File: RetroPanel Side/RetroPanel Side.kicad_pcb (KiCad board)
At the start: 2 copper layers, 100 x 25 mm, 13 parts, among them M1 Mounting_Pin, M10 Mounting_Pad, M11 Mounting_Pad, M12 Mounting_Pad, M13 Mounting_Pad, M2 Mounting_Pin, M3 Mounting_Pin, M4 Mounting_Pad, M5 Mounting_Pad, M6 Mounting_Pad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

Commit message: Rough layout of module
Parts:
- moved M10 4.85 mm to (103.8, 98.5), turned to 270 degrees
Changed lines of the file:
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@@
   )
   (module RetroPanel:Pad_pin (layer F.Cu)
-    (at 103.0916 93.6898 180)
+    (at 103.8155 98.4904 270)
     (descr "module 1 pin (ou trou mecanique de percage)")
     (tags DEV)
-    (fp_text reference M10 (at 0 -4.445) (layer F.Fab) hide
+    (fp_text reference M10 (at 0 -4.445 90) (layer F.Fab) hide
       (effects (font (size 1 1) (thickness 0.15)))
     )
-    (fp_text value Mounting_Pad (at 0 -3.175) (layer F.Fab) hide
+    (fp_text value Mounting_Pad (at 0 -3.175 90) (layer F.Fab) hide
       (effects (font (size 1 1) (thickness 0.15)))
     )
-    (pad 1 smd rect (at 0 0 180) (size 3 4.4) (layers B.Cu B.Paste B.Mask)
+    (pad 1 smd rect (at 0 0 270) (size 3 4.4) (layers B.Cu B.Paste B.Mask)
       (net 1 GND))
-    (pad 1 smd rect (at 0 0 180) (size 3 4.4) (layers F.Cu F.Paste F.Mask)
+    (pad 1 smd rect (at 0 0 270) (size 3 4.4) (layers F.Cu F.Paste F.Mask)
       (net 1 GND))
   )
@@
       (effects (font (size 1 1) (thickness 0.15)))
     )
+    (fp_circle (center 0 0) (end 2.6 0) (layer F.CrtYd) (width 0.05))
     (fp_circle (center 0 0) (end 2 0.8) (layer F.Fab) (width 0.1))
-    (fp_circle (center 0 0) (end 2.6 0) (layer F.CrtYd) (width 0.05))
     (pad 1 thru_hole circle (at 0 0) (size 3.5 3.5) (drill 3.048) (layers *.Cu *.Mask)
       (net 1 GND) (solder_mask_margin 0.8))
@@
       (effects (font (size 1 1) (thickness 0.15)))
     )
+    (fp_circle (center 0 0) (end 2 0.8) (layer F.Fab) (width 0.1))
     (fp_circle (center 0 0) (end 2.6 0) (layer F.CrtYd) (width 0.05))
-    (fp_circle (center 0 0) (end 2 0.8) (layer F.Fab) (width 0.1))
     (pad 1 thru_hole circle (at 0 0) (size 3.5 3.5) (drill 3.048) (layers *.Cu *.Mask)
       (net 1 GND) (solder_mask_margin 0.8))
@@
       (effects (font (size 1 1) (thickness 0.15)))
     )
+    (fp_circle (center 0 0) (end 2 0.8) (layer F.Fab) (width 0.1))
     (fp_circle (center 0 0) (end 2.6 0) (layer F.CrtYd) (width 0.05))
-    (fp_circle (center 0 0) (end 2 0.8) (layer F.Fab) (width 0.1))
     (pad 1 thru_hole circle (at 0 0) (size 3.5 3.5) (drill 3.048) (layers *.Cu *.Mask)
       (net 1 GND) (solder_mask_margin 0.8))

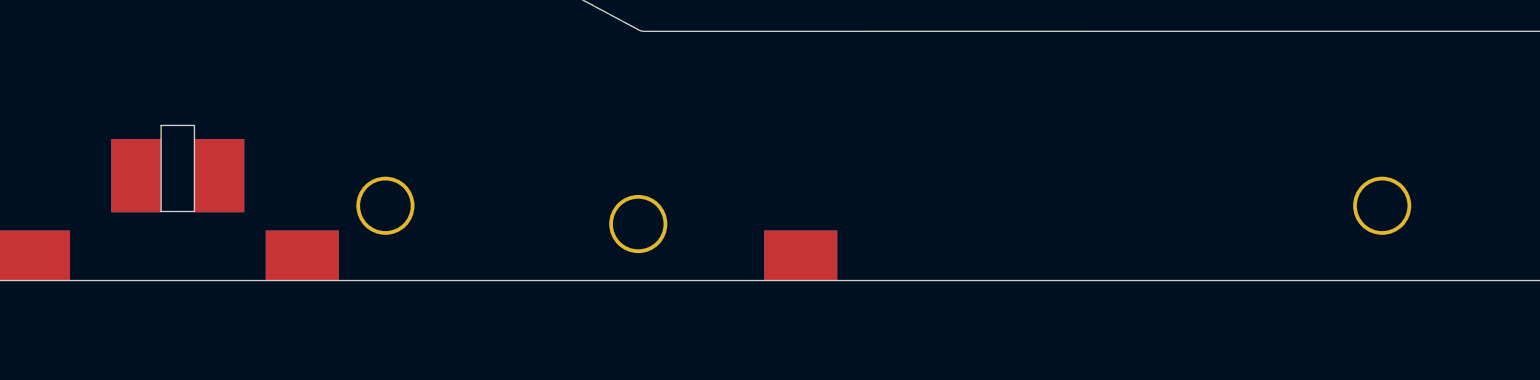
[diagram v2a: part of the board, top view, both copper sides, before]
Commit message: Adjustable mounting with huge pads
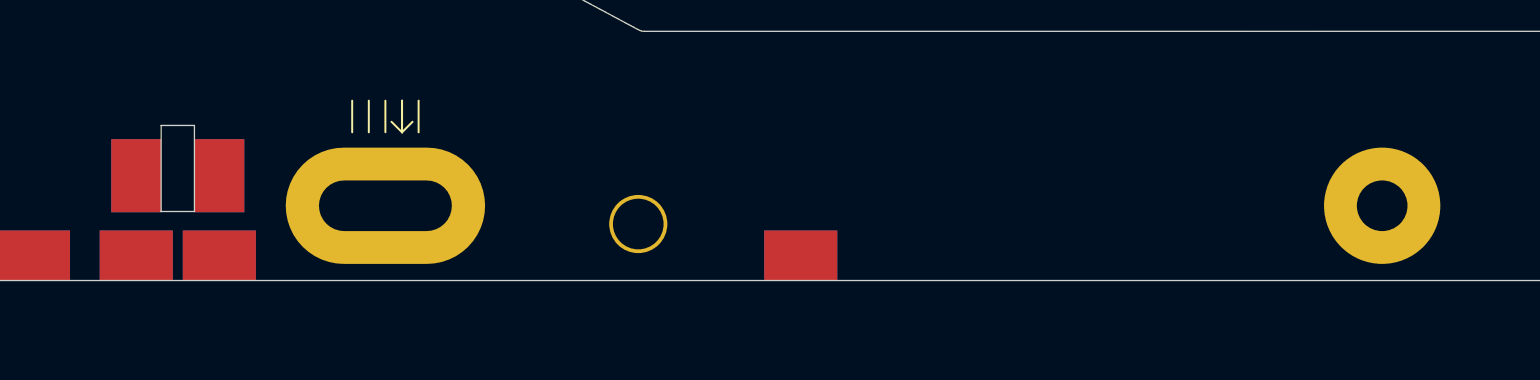
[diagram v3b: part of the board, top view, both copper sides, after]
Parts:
- added M14: Mounting_Pad, RetroPanel:Pad_pin, F.Cu at (110.0, 98.5)
- M1: footprint mounting:M3_pin -> mounting:M3_adjustable
- M2: footprint mounting:M3_pin -> mounting:M3_big
- moved M6 5.00 mm to (115.0, 98.5)
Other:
- board text added: "RetroPanel Side (rev. B) github.com/tebl"
- board text removed: "RetroPanel Side (rev. A) github.com/tebl"

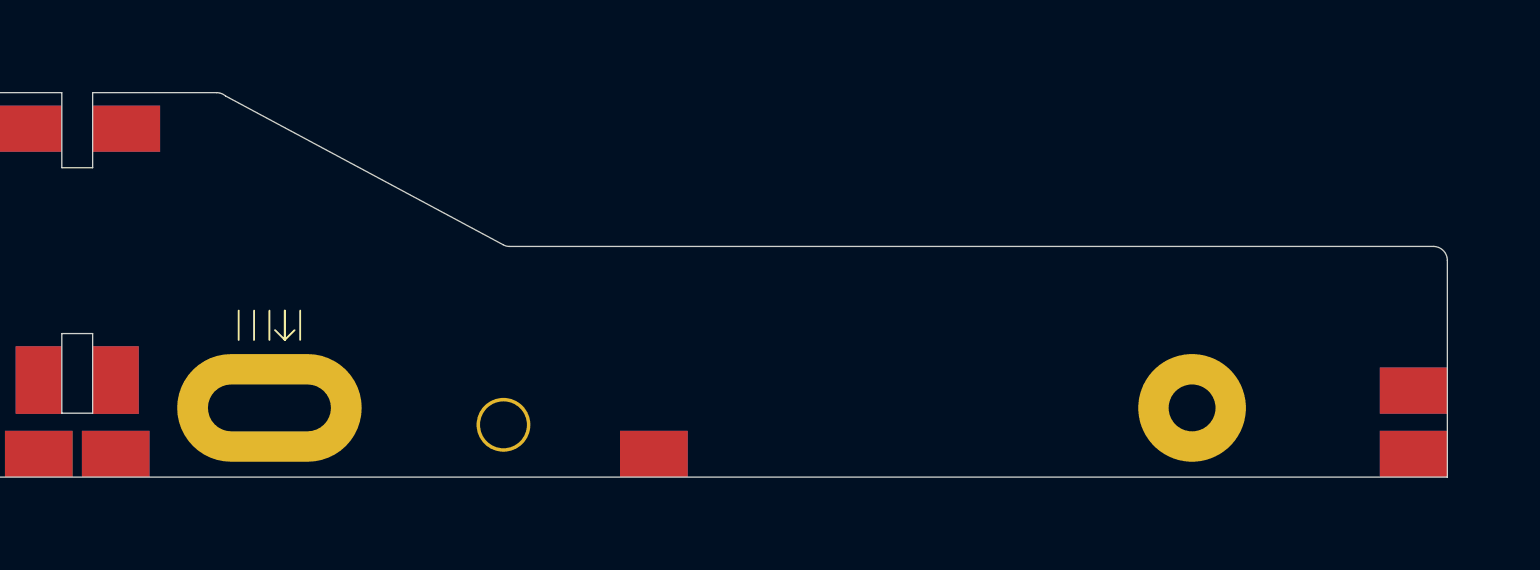
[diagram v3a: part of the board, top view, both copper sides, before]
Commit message: Fixed RS-232 connector and export files for second prototype
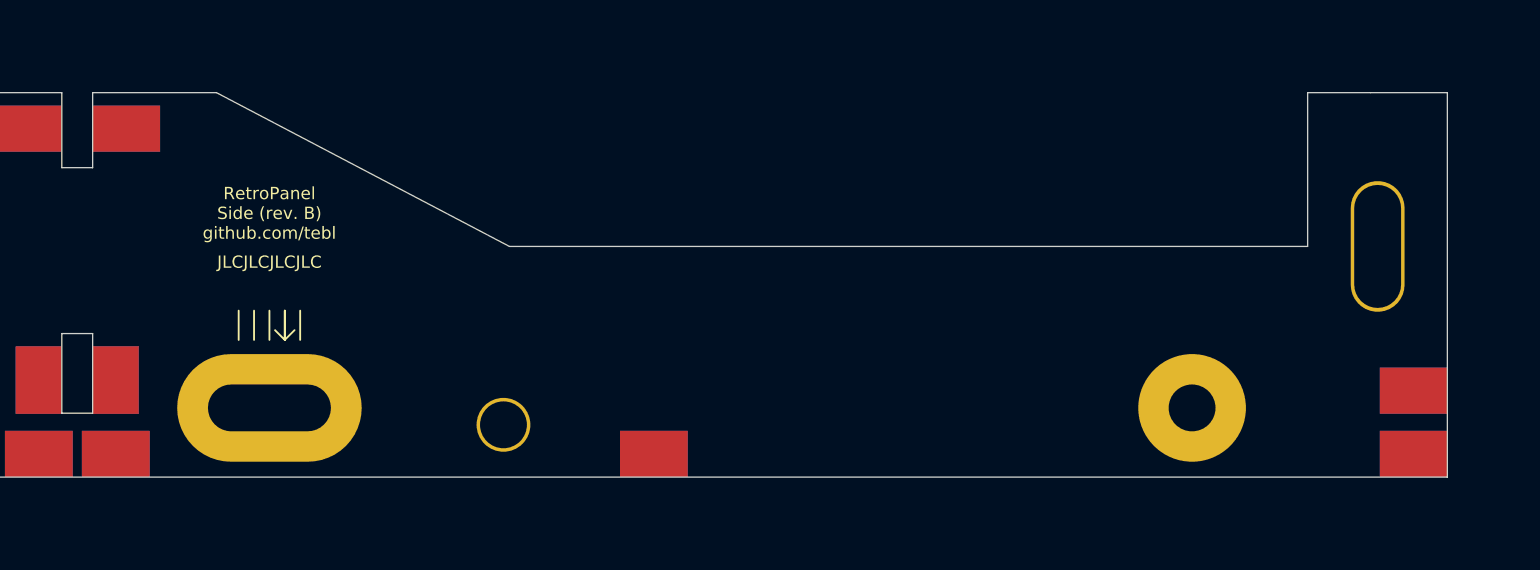
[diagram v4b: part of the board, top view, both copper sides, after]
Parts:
- added M15: Mounting_Pin, mounting:M3_pin_wide, F.Cu at (197.1, 85.0)
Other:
- outline, holes or cut-outs redrawn
- board text added: "JLCJLCJLCJLC"

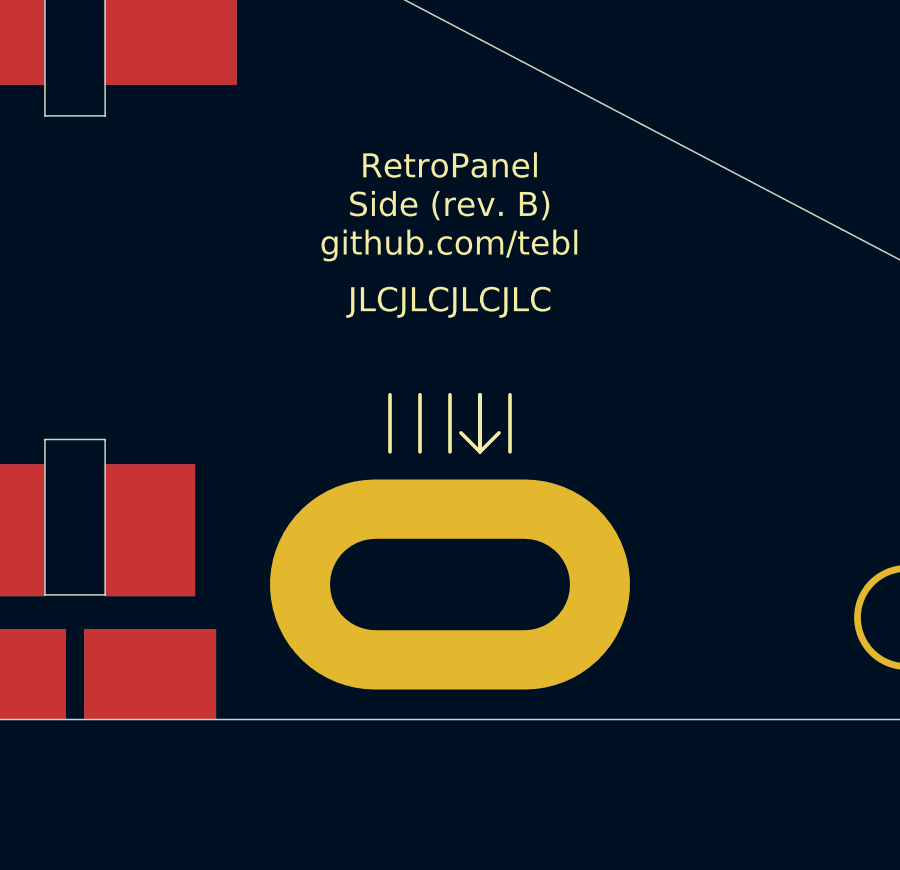
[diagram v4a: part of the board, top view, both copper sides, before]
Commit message: Adjust cutout to move unit forward
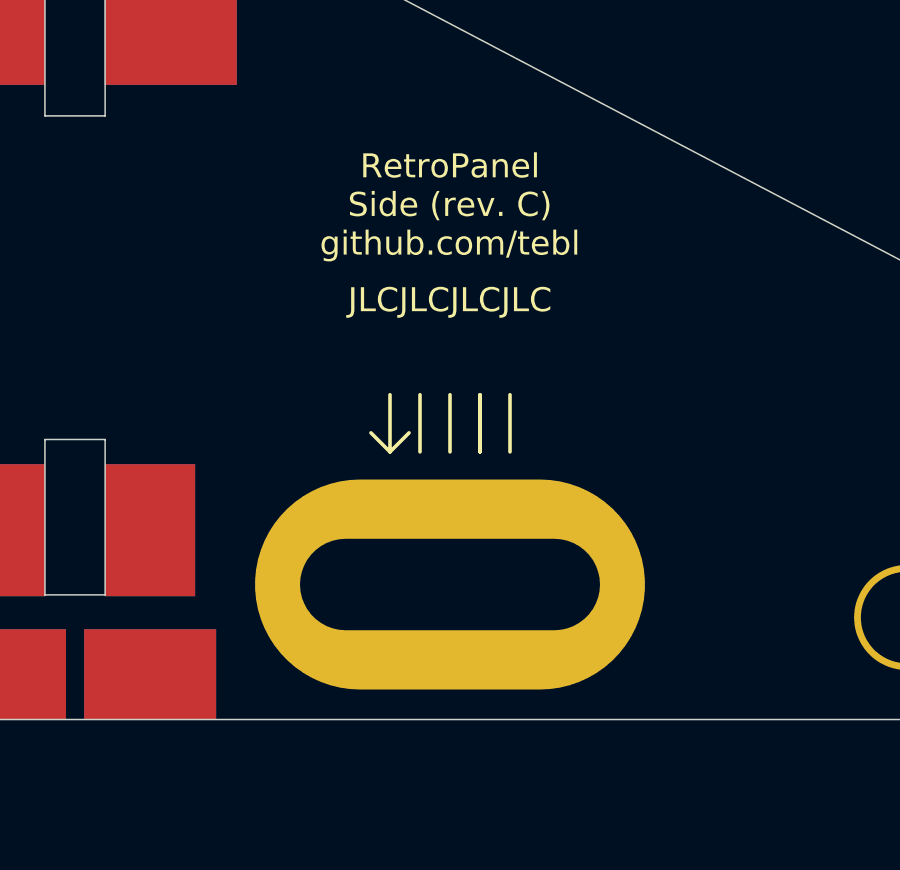
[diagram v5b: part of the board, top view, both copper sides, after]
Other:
- board text added: "RetroPanel Side (rev. C) github.com/tebl"
- board text removed: "RetroPanel Side (rev. B) github.com/tebl"
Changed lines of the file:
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@@
     (fp_circle (center 0 0) (end 2.6 0) (layer F.CrtYd) (width 0.05))
     (fp_circle (center 0 0) (end 2 0.8) (layer F.Fab) (width 0.1))
-    (pad 1 thru_hole oval (at 0 0) (size 12 7) (drill oval 8 3.048) (layers *.Cu *.Mask)
+    (pad 1 thru_hole oval (at 0 0) (size 13 7) (drill oval 10 3.048) (layers *.Cu *.Mask)
       (net 1 GND) (solder_mask_margin 0.8))
   )
@@
       (effects (font (size 1 1) (thickness 0.15)))
     )
-    (fp_circle (center 0 0) (end 2 0.8) (layer F.Fab) (width 0.1))
     (fp_circle (center 0 0) (end 2.6 0) (layer F.CrtYd) (width 0.05))
+    (fp_circle (center 0 0) (end 2 0.8) (layer F.Fab) (width 0.1))
     (pad 1 thru_hole circle (at 0 0) (size 3.5 3.5) (drill 3.048) (layers *.Cu *.Mask)
       (net 1 GND) (solder_mask_margin 0.8))
@@
       (effects (font (size 1 1) (thickness 0.15)))
     )
+    (fp_circle (center 0 0) (end 2 0.8) (layer F.Fab) (width 0.1))
     (fp_circle (center 0 0) (end 2.6 0) (layer F.CrtYd) (width 0.05))
-    (fp_circle (center 0 0) (end 2 0.8) (layer F.Fab) (width 0.1))
     (pad 1 thru_hole oval (at 0 0) (size 7 7) (drill 3.048) (layers *.Cu *.Mask)
       (net 1 GND) (solder_mask_margin 0.8))
@@
       (net 1 GND) (solder_mask_margin 0.8))
   )
+  (gr_line (start 123 91.079) (end 122.365 90.444) (layer F.SilkS) (width 0.12))
+  (gr_line (start 123 91.079) (end 123.635 90.444) (layer B.SilkS) (width 0.12))
+  (gr_line (start 123 91.079) (end 123.635 90.444) (layer F.SilkS) (width 0.12))
+  (gr_line (start 123 91.079) (end 122.365 90.444) (layer B.SilkS) (width 0.12))
   (gr_text JLCJLCJLCJLC (at 125 86.019) (layer F.SilkS)
     (effects (font (size 0.8 0.8) (thickness 0.1)))
@@
   (gr_line (start 127 91.079) (end 127 89.174) (layer F.SilkS) (width 0.12))
   (gr_line (start 127 91.079) (end 127 89.174) (layer B.SilkS) (width 0.12))
-  (gr_line (start 126 91.079) (end 126.635 90.444) (layer F.SilkS) (width 0.12))
-  (gr_line (start 126 91.079) (end 125.365 90.444) (layer B.SilkS) (width 0.12))
   (gr_line (start 126 91.079) (end 126 89.174) (layer B.SilkS) (width 0.12))
-  (gr_line (start 126 91.079) (end 126.635 90.444) (layer B.SilkS) (width 0.12))
-  (gr_line (start 126 91.079) (end 125.365 90.444) (layer F.SilkS) (width 0.12))
   (gr_line (start 126 91.079) (end 126 89.174) (layer F.SilkS) (width 0.12))
   (gr_line (start 140.61 84.999999) (end 121.56 75) (layer Edge.Cuts) (width 0.05))
@@
   (gr_line (start 101.6 97.4998) (end 101.6 95.8998) (layer Dwgs.User) (width 0.05))
   (gr_line (start 201.6 95.899) (end 101.6 95.8998) (layer Dwgs.User) (width 0.05))
-  (gr_text "RetroPanel\nSide (rev. B)\ngithub.com/tebl" (at 125 82.844) (layer F.SilkS)
+  (gr_text "RetroPanel\nSide (rev. C)\ngithub.com/tebl" (at 125 82.844) (layer F.SilkS)
     (effects (font (size 0.8 0.8) (thickness 0.1)))
   )
